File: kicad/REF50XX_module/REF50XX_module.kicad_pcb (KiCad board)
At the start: 2 copper layers, 20.8 x 15.7 mm, 11 parts, among them J1 PINS_1X6, J2 PINS_1X6, U1 REF50X0

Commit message: * more PCB layout stuff
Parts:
- J1, J2: moved to B.Cu
- moved R3 12.2 mm to (130.5, 86.4), turned to 180 degrees
- moved R2 9.78 mm to (150.7, 78.5), turned to 180 degrees
- moved C1 4.71 mm to (129.3, 78.5), turned to 90 degrees
- moved RV1 4.60 mm to (134.7, 86.5), turned to 270 degrees
- moved C3 4.04 mm to (142.0, 79.5), turned to 270 degrees
- moved C4 2.41 mm to (139.7, 79.5)
- moved R1 2.37 mm to (137.3, 82.0)
- moved C2 2.37 mm to (134.3, 81.5)
- moved U1 2.19 mm to (134.4, 77.9)
- turned J1 to 90 degrees
- turned J2 to 270 degrees

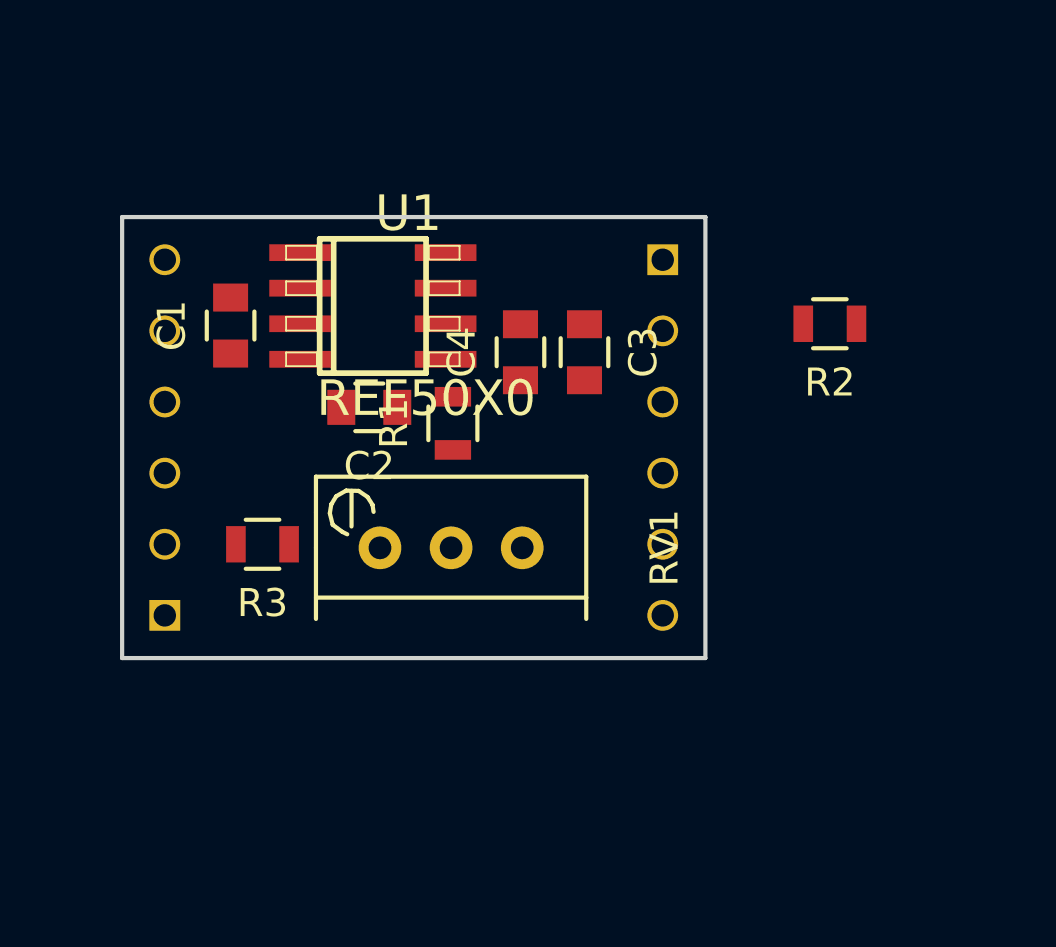
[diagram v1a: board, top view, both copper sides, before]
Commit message: * Some more layouting of the REF50XX module
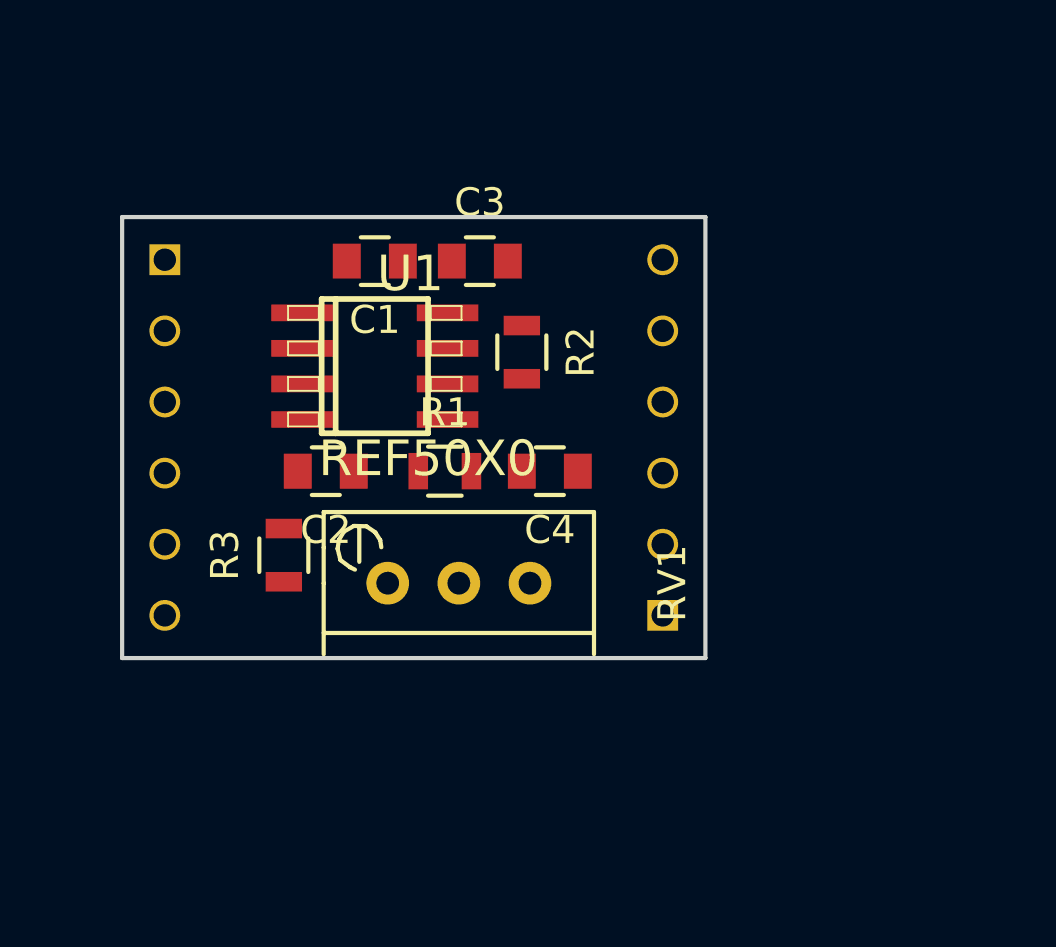
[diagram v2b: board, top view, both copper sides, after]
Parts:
- moved R2 11.0 mm to (139.8, 79.5), turned to 270 degrees
- moved C1 5.64 mm to (134.5, 76.2), turned to 180 degrees
- moved C3 4.95 mm to (138.2, 76.2), turned to 0 degrees
- moved C4 4.38 mm to (140.8, 83.8), turned to 180 degrees
- moved C2 2.76 mm to (132.8, 83.8)
- moved U1 2.15 mm to (134.5, 80.0)
- moved R1 1.73 mm to (137.0, 83.8), turned to 0 degrees
- moved RV1 1.29 mm to (135.0, 87.8)
- moved R3 0.85 mm to (131.2, 86.8), turned to 90 degrees
- turned J1 to 270 degrees
- turned J2 to 90 degrees
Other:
- rule pad_to_mask_clearance: 0.2 -> 0.1

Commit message: * redid partially REF5040 reference board
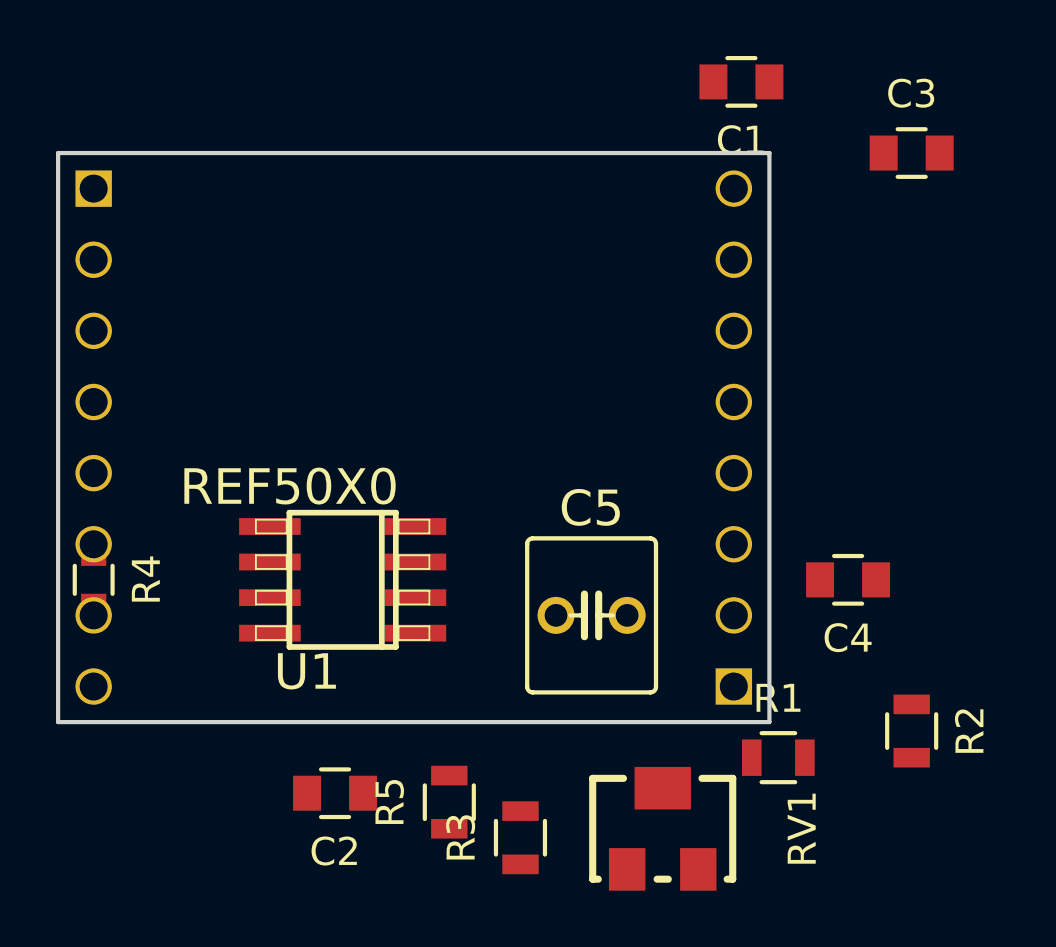
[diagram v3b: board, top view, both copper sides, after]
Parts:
- added C5: 4.7u, SquantorRcl:C025-055X046, F.Cu at (142.2, 88.9)
- added R4: 0, Resistors_SMD:R_0603, F.Cu at (124.5, 87.6)
- added R5: 0, Resistors_SMD:R_0805, F.Cu at (137.2, 95.6)
- J1, J2: value PINS_1X6 -> PINS_1X8; footprint SquantorConnectors:Header-2.54-1X06-H0.8 -> SquantorConnectors:Header-0254-1X08-H010
- RV1: footprint Potentiometers:Potentiometer_Bourns_3296W_3-8Zoll_Inline_ScrewUp -> SquantorRcl:POT_SMD_44W
- moved R2 19.4 mm to (153.7, 93.0)
- moved C3 15.9 mm to (153.7, 72.4)
- moved R1 15.7 mm to (148.9, 94.0)
- moved C1 14.6 mm to (147.6, 69.8)
- moved RV1 13.2 mm to (144.8, 96.5)
- moved R3 13.2 mm to (139.7, 96.8)
- moved C2 11.5 mm to (133.1, 95.2)
- moved C4 11.3 mm to (151.4, 87.6)
- moved U1 7.72 mm to (133.3, 87.6), turned to 90 degrees
- moved J1 2.54 mm to (124.5, 82.5)
- moved J2 2.54 mm to (147.3, 82.5)
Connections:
- C1 pad 2: Net-(C1-Pad2) -> Vin
- C4 pad 2: Net-(C4-Pad2) -> Vref
- J1 pad 1: (no net) -> GND
- J1 pad 2: Net-(C1-Pad2) -> GND
- J1 pad 3: Net-(J1-Pad3) -> GND
- J1 pad 4: (no net) -> GND
- J1 pad 5: (no net) -> GND
- J1 pad 6: GND -> Sense
- J2 pad 2: (no net) -> GND
- J2 pad 3: (no net) -> GND
- J2 pad 4: (no net) -> RefTemp
- J2 pad 5: Net-(C4-Pad2) -> Vin
- J2 pad 6: (no net) -> HeaterGround
- R2 pad 2: Net-(C4-Pad2) -> Vref
- RV1 pad 3: Net-(C4-Pad2) -> Net-(R5-Pad2)
- U1 pad 2: Net-(C1-Pad2) -> Vin
- U1 pad 3: Net-(J1-Pad3) -> RefTemp
- U1 pad 6: Net-(C4-Pad2) -> Vref
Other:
- board size 20.8 x 15.7 mm -> 25.4 x 20.3 mm
